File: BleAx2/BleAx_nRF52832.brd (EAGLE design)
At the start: 30 x 20.1 mm, 42 parts, among them CN1 6p-2.54, J1 2.0MM-90D, U1 NRF52832, U2 MCP73832T-2ACI/OT-SOT23-5, U4 MIC5225-3.3, X1 FA-128, X2 32.768kHz

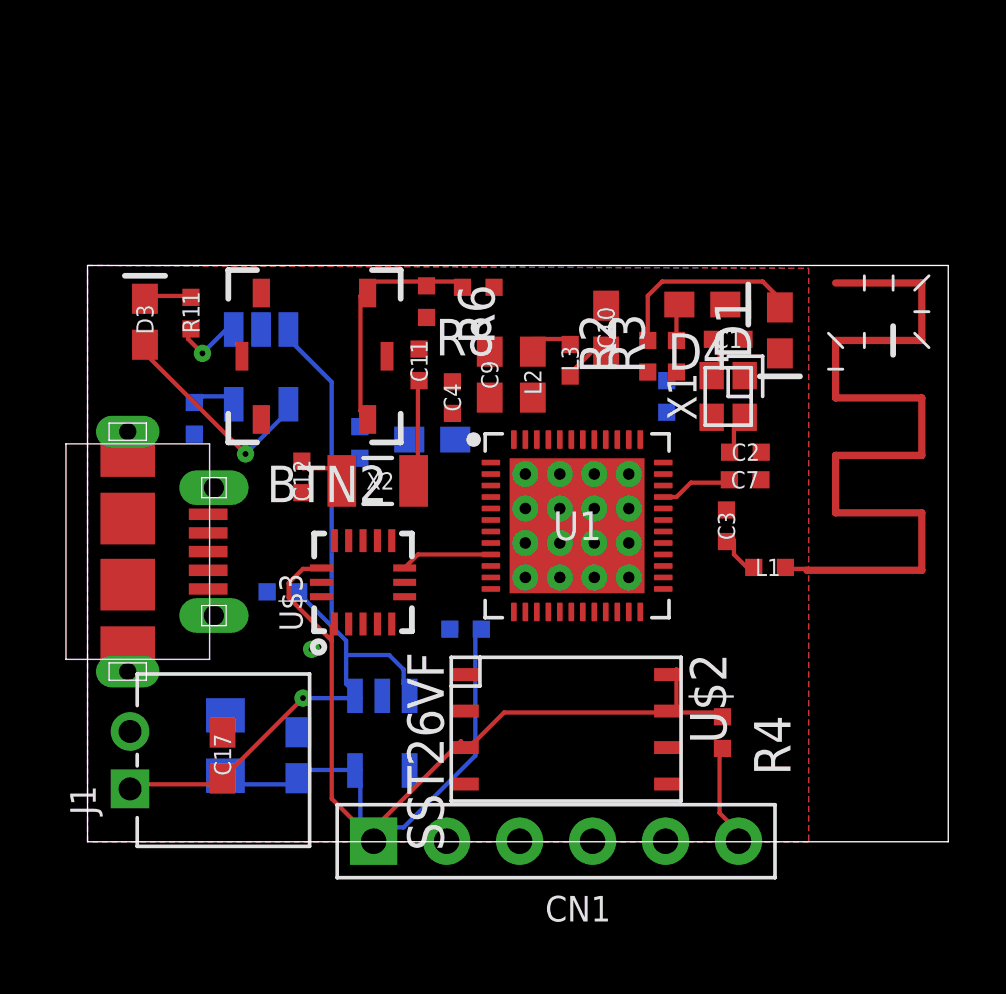
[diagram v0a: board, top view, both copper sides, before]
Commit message: evolve_ button move down
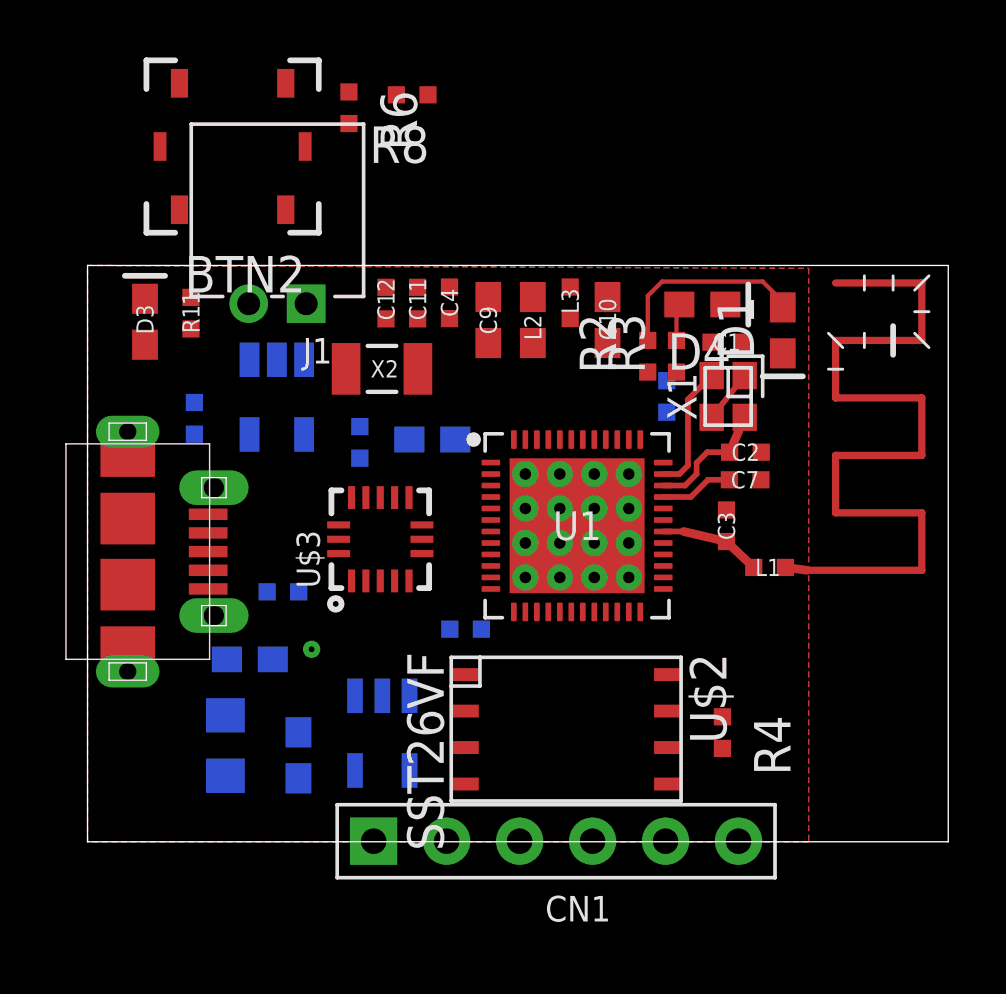
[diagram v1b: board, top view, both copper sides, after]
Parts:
- moved J1 19.2 mm to (6.61, 22.0), turned to 180 degrees
- moved BTN2 7.84 mm to (5.05, 24.2)
- moved R6 7.27 mm to (9.10, 25.6)
- moved R8 7.08 mm to (11.3, 26.0)
- moved C12 6.72 mm to (10.4, 18.8), turned to 270 degrees
- moved X2 3.90 mm to (10.2, 16.5)
- moved C17 3.48 mm to (5.65, 6.35), flipped to the bottom, turned to 0 degrees
- moved C4 3.30 mm to (12.6, 18.8)
- moved C11 2.15 mm to (11.5, 18.8)
- moved L3 2.00 mm to (16.8, 18.8)
- moved C9 1.90 mm to (13.9, 18.2)
- moved L2 1.90 mm to (15.5, 18.2)
- moved U$3 1.62 mm to (10.2, 10.5)
- moved U2 1.19 mm to (6.59, 15.5)
- moved C10 0.30 mm to (18.1, 18.2)
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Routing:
- net VDD_P3V3: track 46.2 -> 0.23 mm
- net VDD_BATT: track 28.3 -> 0.00 mm, vias 1 -> 0
- net N$6: track 8.59 -> 0.00 mm
- net VCC_P5V0_USB: track 7.60 -> 0.00 mm, vias 1 -> 0
- net XL1: track 3.53 -> 0.00 mm
- net P0.21/RESET: track 3.48 -> 0.00 mm
- net LIS_CS: track 3.30 -> 0.00 mm
- net N$10: track 2.99 -> 0.00 mm, vias 1 -> 0
- net N$3: track 1.64 -> 4.45 mm
- net X1: track 1.63 -> 4.34 mm
- net N$2: track 2.22 -> 0.00 mm
- net DEC4: track 2.21 -> 0.00 mm
- net ANT: track 1.67 -> 3.55 mm
- net XL2: track 1.82 -> 0.00 mm
- net N$9: track 1.71 -> 0.00 mm
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
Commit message: halfway?
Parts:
- moved R6 23.3 mm to (5.40, 2.55), turned to 90 degrees
- moved BTN2 20.1 mm to (9.10, 4.50)
- moved R8 18.5 mm to (12.8, 7.60), turned to 270 degrees
- moved C17 2.28 mm to (7.85, 6.95)
- moved U$3 1.27 mm to (9.64, 11.7)
- moved C6 1.08 mm to (7.74, 4.01)
- moved C9 0.90 mm to (13.9, 17.3)
- moved C19 0.82 mm to (5.30, 4.05)
- moved C10 0.80 mm to (18.1, 17.4)
- moved R4 0.78 mm to (22.7, 3.30)
- moved U$2 0.70 mm to (17.5, 4.10)
- moved U4 0.65 mm to (10.9, 4.03)
- moved C5 0.51 mm to (13.4, 6.95)
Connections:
- net BTTN_01: now also U1.12; no longer U1.43
- net LIS_CS: now also U1.8; no longer U1.9
- net LIS_INT1: now also U1.7; no longer U1.8
- net MISO_01: now also U1.9; no longer U1.10
- net MOSI_01: now also U1.10; no longer U1.11
- net SCK_01: now also U1.11; no longer U1.12
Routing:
- net VDD_P3V3: track 0.23 -> 17.2 mm, vias 0 -> 3
- net XL2: track 0.00 -> 9.33 mm
- net GND: track 1.85 -> 10.6 mm, vias 0 -> 23
- net LIS_INT1: track 0.00 -> 7.06 mm
- net XL1: track 0.00 -> 6.83 mm
- net DEC4: track 0.00 -> 6.02 mm
- net DEC1: track 0.00 -> 5.81 mm
- net SCK_01: track 0.00 -> 4.71 mm
- net LED_02: track 0.00 -> 4.41 mm
- net LED_01: track 0.00 -> 4.16 mm
- net LIS_CS: track 0.00 -> 4.00 mm
- net MISO_01: track 0.00 -> 3.94 mm
- net MOSI_01: track 0.00 -> 3.94 mm
- net N$4: track 0.00 -> 3.47 mm
- net N$2: track 0.00 -> 1.35 mm
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
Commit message: half half evolve
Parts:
- D1: value LED -> LED_BLUE
- D3: value LED -> LED_CHARGE
- D4: value LED -> LED_GREEN
- moved C13 0.22 mm to (9.30, 14.0), turned to 180 degrees
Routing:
- net VDD_P3V3: track 17.2 -> 27.1 mm, vias 3 -> 5
- net GND: track 10.6 -> 14.6 mm, vias 23 -> 26
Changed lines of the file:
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@@
 <layer number="14" name="Route14" color="1" fill="6" visible="no" active="no"/>
 <layer number="15" name="Route15" color="4" fill="6" visible="no" active="no"/>
-<layer number="16" name="Bottom" color="1" fill="1" visible="yes" active="yes"/>
+<layer number="16" name="Bottom" color="1" fill="1" visible="no" active="yes"/>
 <layer number="17" name="Pads" color="2" fill="1" visible="yes" active="yes"/>
 <layer number="18" name="Vias" color="2" fill="1" visible="yes" active="yes"/>
@@
 <attribute name="VALUE" x="8.39" y="19.45" size="1.27" layer="27" rot="R270"/>
 </element>
-<element name="D3" library="Nordic_misc" package="DIOC0603_N" value="LED" x="2" y="18.1" smashed="yes" rot="R270">
+<element name="D3" library="Nordic_misc" package="DIOC0603_N" value="LED_CHARGE" x="2" y="18.1" smashed="yes" rot="R270">
 <attribute name="NAME" x="1.7" y="18.7" size="0.6" layer="25" rot="R270"/>
 <attribute name="VALUE" x="-0.5" y="19.1" size="1.27" layer="27" rot="R270"/>
@@
 <attribute name="MPN" value="F185-1106A1BSYC1" x="16.31" y="0.02" size="1.778" layer="27" rot="R90" display="off"/>
 </element>
-<element name="C13" library="Nordic_misc" package="RESC0402_N" value="100nF" x="9.48" y="13.9" rot="MR90"/>
+<element name="C13" library="Nordic_misc" package="RESC0402_N" value="100nF" x="9.3" y="14.02" rot="MR180"/>
 <element name="U4" library="microbuilder" package="SOT23-5" value="MIC5225-3.3" x="10.86" y="4.03" rot="MR180"/>
 <element name="U2" library="Seeed-OPL-ic" package="SOT-23-5" value="MCP73832T-2ACI/OT-SOT23-5" x="6.59" y="15.48" rot="MR180">
@@
 <element name="J1" library="Seeed-OPL-Connector" package="H2-2.0-90D" value="2.0MM-90D" x="6.61" y="21.98" rot="R180"/>
 <element name="U$2" library="sst26" package="SOIJ8" value="SST26VF" x="17.5" y="4.1" rot="R270"/>
-<element name="D1" library="Nordic_misc" package="DIOC0603_N" value="LED" x="24.2" y="17.8" rot="R90"/>
+<element name="D1" library="Nordic_misc" package="DIOC0603_N" value="LED_BLUE" x="24.2" y="17.8" rot="R90"/>
 <element name="R2" library="Nordic_misc" package="RESC0402_N" value="1k" x="19.5" y="16.9" rot="R90"/>
-<element name="D4" library="Nordic_misc" package="DIOC0603_N" value="LED" x="21.4" y="18.7" rot="R180"/>
+<element name="D4" library="Nordic_misc" package="DIOC0603_N" value="LED_GREEN" x="21.4" y="18.7" rot="R180"/>
 <element name="R3" library="Nordic_misc" package="RESC0402_N" value="1k" x="20.5" y="16.9" rot="R90"/>
 <element name="U$1" library="con-molex-usb" package="47589-0001" value="MICRO-USB-RECEPTACLE47589-0001" x="1.4" y="10.1"/>
@@
 <wire x1="22.8" y1="17.39" x2="22.8" y2="18.1" width="0.3048" layer="1"/>
 <wire x1="22.8" y1="18.1" x2="22.2" y2="18.7" width="0.3048" layer="1"/>
+<via x="21.35" y="13.9" extent="1-16" drill="0.2"/>
+<via x="9.25" y="12" extent="1-16" drill="0.2"/>
+<via x="9.95" y="11.3" extent="1-16" drill="0.2"/>
+<via x="11.35" y="9.9" extent="1-16" drill="0.2"/>
+<wire x1="10.14" y1="13.13" x2="10.14" y2="11.49" width="0.2" layer="1"/>
+<wire x1="10.14" y1="11.49" x2="9.95" y2="11.3" width="0.2" layer="1"/>
+<wire x1="9.14" y1="13.13" x2="9.14" y2="12.11" width="0.2" layer="1"/>
+<wire x1="9.14" y1="12.11" x2="9.25" y2="12" width="0.2" layer="1"/>
+<wire x1="10.64" y1="10.23" x2="10.97" y2="9.9" width="0.2" layer="1"/>
+<wire x1="10.97" y1="9.9" x2="11.35" y2="9.9" width="0.2" layer="1"/>
 <wire x1="24.25" y1="14.8" x2="24.25" y2="15.8" width="0" layer="19" extent="1-1"/>
 <wire x1="24.2" y1="17" x2="24.25" y2="15.8" width="0" layer="19" extent="1-1"/>
+<wire x1="21.35" y1="13.9" x2="21.725" y2="14.775" width="0" layer="19" extent="1-1"/>
 <wire x1="24.45" y1="13.6" x2="24.25" y2="14.8" width="0" layer="19" extent="1-1"/>
 <wire x1="23.45" y1="13.56" x2="24.45" y2="13.6" width="0" layer="19" extent="1-1"/>
@@
 <wire x1="1.25" y1="2.8" x2="1.15" y2="4.1" width="0" layer="19" extent="1-1"/>
 <wire x1="0.95" y1="1.4" x2="1.25" y2="2.8" width="0" layer="19" extent="1-1"/>
+<wire x1="11.35" y1="9.9" x2="12.860003125" y2="6.950959375" width="0" layer="19" extent="16-16"/>
+<wire x1="9.95" y1="11.3" x2="10.64" y2="10.23" width="0" layer="19" extent="1-1"/>
+<wire x1="9.25" y1="12" x2="9.95" y2="11.3" width="0" layer="19" extent="1-1"/>
+<wire x1="11.2" y1="14" x2="10.14" y2="13.13" width="0" layer="19" extent="1-16"/>
+<wire x1="9.85" y1="14.02" x2="9.14" y2="13.13" width="0" layer="19" extent="1-16"/>
 <wire x1="14.35" y1="19.4" x2="17.75" y2="19.4" width="0" layer="19" extent="1-1"/>
 <wire x1="13.45" y1="19.4" x2="14.35" y2="19.4" width="0" layer="19" extent="1-1"/>
 <wire x1="12.59" y1="19.3" x2="13.45" y2="19.4" width="0" layer="19" extent="1-1"/>
 <wire x1="13.95" y1="18.06" x2="14.35" y2="19.4" width="0" layer="19" extent="1-1"/>
-<wire x1="10.64" y1="10.23" x2="12.860003125" y2="6.950959375" width="0" layer="19" extent="1-16"/>
-<wire x1="10.14" y1="13.13" x2="10.64" y2="10.23" width="0" layer="19" extent="1-1"/>
-<wire x1="9.14" y1="13.13" x2="10.14" y2="13.13" width="0" layer="19" extent="1-1"/>
-<wire x1="11.2" y1="14" x2="10.14" y2="13.13" width="0" layer="19" extent="1-16"/>
-<wire x1="9.48" y1="14.45" x2="9.14" y2="13.13" width="0" layer="19" extent="1-16"/>
-<wire x1="6.59" y1="16.7801" x2="9.48" y2="14.45" width="0" layer="19" extent="16-16"/>
+<wire x1="6.59" y1="16.7801" x2="9.85" y2="14.02" width="0" layer="19" extent="16-16"/>
 <wire x1="5.61" y1="18.73" x2="6.59" y2="16.7801" width="0" layer="19" extent="16-16"/>
 <wire x1="3.72" y1="14.19" x2="6.59" y2="16.7801" width="0" layer="19" extent="16-16"/>
-<via x="21.35" y="13.9" extent="1-16" drill="0.2"/>
 </signal>
 <signal name="DEC1">
@@
 <wire x1="20" y1="14" x2="20.16" y2="14.95" width="0.2" layer="16"/>
 <wire x1="14" y1="14" x2="13.95" y2="16.46" width="0.3048" layer="1"/>
+<via x="7.8" y="12.9" extent="1-16" drill="0.2"/>
+<wire x1="7.8" y1="12.9" x2="8.4" y2="12.9" width="0.2" layer="16"/>
+<wire x1="8.4" y1="12.9" x2="8.7" y2="13.2" width="0.2" layer="16"/>
+<wire x1="8.7" y1="13.2" x2="8.7" y2="13.97" width="0.2" layer="16"/>
+<wire x1="8.7" y1="13.97" x2="8.75" y2="14.02" width="0.2" layer="16"/>
+<via x="7.8" y="10.2" extent="1-16" drill="0.2"/>
+<wire x1="7.8" y1="10.2" x2="7.8" y2="12.9" width="0.3048" layer="16"/>
+<wire x1="7.8" y1="10.2" x2="7.4" y2="10.2" width="0.2" layer="1"/>
+<wire x1="7.4" y1="10.2" x2="7.1" y2="10.5" width="0.2" layer="1"/>
+<wire x1="7.1" y1="10.5" x2="7.1" y2="12.2" width="0.2" layer="1"/>
+<wire x1="8.17" y1="12.2" x2="7.1" y2="12.2" width="0.2" layer="1"/>
+<wire x1="8.19" y1="12.18" x2="8.17" y2="12.2" width="0.2" layer="1"/>
+<wire x1="8.19" y1="12.18" x2="8.19" y2="12.51" width="0.2" layer="1"/>
+<wire x1="8.19" y1="12.51" x2="7.8" y2="12.9" width="0.2" layer="1"/>
+<wire x1="8.64" y1="10.23" x2="7.83" y2="10.23" width="0.2" layer="1"/>
+<wire x1="7.83" y1="10.23" x2="7.8" y2="10.2" width="0.2" layer="1"/>
 <wire x1="14" y1="14" x2="14.84" y2="14" width="0" layer="19" extent="1-16"/>
 <wire x1="13.96" y1="6.9490375" x2="13.9" y2="8" width="0" layer="19" extent="16-16"/>
 <wire x1="12.8" y1="14" x2="14" y2="14" width="0" layer="19" extent="16-16"/>
-<wire x1="9.48" y1="13.35" x2="12.8" y2="14" width="0" layer="19" extent="16-16"/>
-<wire x1="8.19" y1="12.18" x2="9.48" y2="13.35" width="0" layer="19" extent="1-16"/>
-<wire x1="8.64" y1="10.23" x2="8.19" y2="12.18" width="0" layer="19" extent="1-1"/>
 <wire x1="13.77" y1="3.53" x2="13.96" y2="6.9490375" width="0" layer="19" extent="1-16"/>
 <wire x1="9.91" y1="2.7299" x2="13.77" y2="3.53" width="0" layer="19" extent="1-16"/>
@@
 <wire x1="5.3" y1="2.95" x2="5.4" y2="3.1" width="0" layer="19" extent="1-16"/>
 <wire x1="9.96" y1="0.02" x2="9.91" y2="2.7299" width="0" layer="19" extent="16-16"/>
+<wire x1="8.75" y1="14.02" x2="12.8" y2="14" width="0" layer="19" extent="16-16"/>
 <wire x1="20.87" y1="6.07" x2="14.84" y2="8" width="0" layer="19" extent="1-1"/>
 <wire x1="20.87" y1="4.8" x2="20.87" y2="6.07" width="0" layer="19" extent="1-1"/>
@@
 <contactref element="U$3" pad="11"/>
 <contactref element="U1" pad="7"/>
-<wire x1="9.64" y1="13.13" x2="9.64" y2="13.64" width="0.2" layer="1"/>
-<wire x1="9.64" y1="13.64" x2="9.9" y2="13.9" width="0.2" layer="1"/>
-<wire x1="9.9" y1="13.9" x2="10.9" y2="13.9" width="0.2" layer="1"/>
-<wire x1="10.9" y1="13.9" x2="11.2" y2="13.6" width="0.2" layer="1"/>
-<wire x1="11.2" y1="13.6" x2="11.2" y2="12.9" width="0.2" layer="1"/>
-<wire x1="11.2" y1="12.9" x2="11.3" y2="12.8" width="0.2" layer="1"/>
-<wire x1="11.3" y1="12.8" x2="12" y2="12.8" width="0.2" layer="1"/>
-<wire x1="12" y1="12.8" x2="13.2" y2="11.6" width="0.2" layer="1"/>
+<wire x1="9.64" y1="13.13" x2="9.64" y2="13.74" width="0.2" layer="1"/>
+<wire x1="9.64" y1="13.74" x2="9.9" y2="14" width="0.2" layer="1"/>
+<wire x1="9.9" y1="14" x2="10.8" y2="14" width="0.2" layer="1"/>
+<wire x1="10.8" y1="14" x2="13.2" y2="11.6" width="0.2" layer="1"/>
 <wire x1="13.2" y1="11.6" x2="13.2" y2="11" width="0.2" layer="1"/>
 <wire x1="13.2" y1="11" x2="13.4" y2="10.8" width="0.2" layer="1"/>
